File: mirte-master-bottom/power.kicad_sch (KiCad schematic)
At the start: 14 parts, among them J10 charger, J11 switch, J3 battery, K2 SANYOU_SRD_Form_A, U1 INA226, U2 TPS82130

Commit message: verder v3 pcb
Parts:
- removed K2: SANYOU_SRD_Form_A, Relay_THT:Relay_SPST_SANYOU_SRD_Series_Form_A, symbol Relay:SANYOU_SRD_Form_A
- added C10: 1000uF, Capacitor_THT:CP_Radial_D10.0mm_P3.50mm, symbol Device:C_Polarized
- added C8: 10uF, Capacitor_SMD:C_0805_2012Metric, symbol Device:C
- added C9: 100nF, Capacitor_SMD:C_0805_2012Metric, symbol Device:C
- added D2, D3: LED, LED_SMD:LED_0805_2012Metric, symbol Device:LED
- added F4: Polyfuse, Fuse:Fuse_1812_4532Metric, symbol Device:Polyfuse
- added J12: USB_A, Connector_USB:USB_A_Molex_67643_Horizontal, symbol Connector:USB_A
- added J2: Conn_02x02_Odd_Even, easyeda2:mini560, symbol Connector_Generic:Conn_02x02_Odd_Even
- added Q3: SiA449DJ, Package_TO_SOT_SMD:Vishay_PowerPAK_SC70-6L_Single, symbol Transistor_FET:SiA449DJ
- added Q5: Si2302CDS-T1-GE3, easyeda2:SOT-23_L2.9-W1.3-P1.90-LS2.4-BR, symbol easyeda:Si2302CDS-T1-GE3
- added R32, R33: 10k, Resistor_SMD:R_0805_2012Metric, symbol Device:R
- added R34: 220, Resistor_SMD:R_0805_2012Metric, symbol Device:R
- added R35: 32k, Resistor_SMD:R_0805_2012Metric, symbol Device:R
- added R4: ~700R, Resistor_SMD:R_0805_2012Metric, symbol Device:R
- added R8: ~600R, Resistor_SMD:R_0805_2012Metric, symbol Device:R
- added SW1: SW_DIP_x01, symbol Switch:SW_DIP_x01
- added U10, U11, U3, U4: 726386-2, easyeda2:CONN-TH_726386-2, symbol easyeda:726386-2
- C1, C2, C3, U2: now not fitted
- J11: value switch -> Ext 12v out; now not fitted
- R15: footprint (none) -> Resistor_SMD:R_1206_3216Metric
- R16, R17, R18: footprint (none) -> Resistor_SMD:R_0805_2012Metric; now not fitted
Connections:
- net +12V: now also J11.1 (Pin_1), C10.1, J2.2 (Pin_2), R4.1
- net +5V: now also F4.1, J2.4 (Pin_4)
- net GND: now also J11.2 (Pin_2), U1.1 (A1), U1.2 (A0), C10.2, C8.2, C9.2, D2.1 (K), D3.1 (K), J12.4 (GND), J12.5 (Shield), J2.1 (Pin_1), J2.3 (Pin_3), Q5.2 (S), R33.1, U11.1
- net VIN: now also Q3.4 (S), R32.2, SW1.1, U4.1; no longer R15.1, U1.10 (Vin+), U1.8 (Vbus)
- new net: D2.2 (A), R4.2
- new net: Q3.3 (G), Q5.3 (D), R32.1
- new net: C8.1, C9.1, F4.2, J12.1 (VBUS), R8.1
- new net: Q5.1 (G), R33.2, R34.2, R35.1
- new net: D3.2 (A), R8.2
- new net PWR_IN_SIG: R34.1, U10.1
- new net VIN_SWITCHED: Q3.1 (D), R15.1, R35.2, SW1.2, U1.10 (Vin+), U1.8 (Vbus), U3.1
- no-connect marks 0 -> 3
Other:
- note added: "PWR light"
- note added: "TODO: check pwr req"
- note added: "of de 469 miss?"
- note added: "switch"
- note removed: "TODO: switch"

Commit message: v3 mm: power upd
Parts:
- added C11: 2.2uF, Capacitor_SMD:C_0805_2012Metric, symbol Device:C
- added D4: 3v3, Diode_SMD:D_0805_2012Metric, symbol Device:D_Zener
- added Q2: Si2302CDS-T1-GE3, easyeda2:SOT-23_L2.9-W1.3-P1.90-LS2.4-BR, symbol easyeda:Si2302CDS-T1-GE3
- added U12: TPS2419D, symbol Power_Management:TPS2419D
- R35: value 32k -> 10k
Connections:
- net GND: now also D4.2 (A), U12.1 (RSET), U12.3 (GND), U12.4 (GND)
- net at Q5.1 (G), R33.2, R34.2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: now also D4.1 (K)
- new net: Q2.1 (G), U12.5 (GATE)
- new net: Q2.3 (D), U12.6 (C)
- new net: C11.1, Q2.2 (S), U12.7 (A)
- new net: C11.2, U12.8 (BYP)
- no-connect marks 3 -> 4
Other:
- note added: "10k: VIN>7v 32k if no D4"
- note added: "Idea: On power-on, no energy flowing anywhere SW1 starts the system Q3 switches the main power when Q5 is on Q5 Gate should be around 3v3 if VIN_SWITCHED is high D4 (zener diode) keeps it at max 3v3 When the microcontroller wants to turn off the power, it switches PWR_IN_SIG to low, turnin off Q5, turning off Q3 R33 is to deplete Q5 when VIN_SWITCHED is off R32 is to deplete Q3 when Q3 is off"
- note added: "N MOSFET"
- note added: "P MOSFET"

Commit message: upd main layout v3
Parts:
- removed U10, U11, U3, U4: 726386-2, easyeda2:CONN-TH_726386-2, symbol easyeda:726386-2
- added C12: 100nF, Capacitor_SMD:C_0805_2012Metric, symbol Device:C
- added J18: Conn_01x02_Pin, Connector_JST:JST_XH_B2B-XH-AM_1x02_P2.50mm_Vertical, symbol Connector:Conn_01x02_Pin
- added J19: 5V, Connector_PinHeader_2.54mm:PinHeader_1x02_P2.54mm_Vertical, symbol Connector:Conn_01x02_Pin
- added J20: 12V, Connector_PinHeader_2.54mm:PinHeader_1x02_P2.54mm_Vertical, symbol Connector:Conn_01x02_Pin
- added J21: 3V3, Connector_PinHeader_2.54mm:PinHeader_1x02_P2.54mm_Vertical, symbol Connector:Conn_01x02_Pin
- added J4: VIN, Connector_PinHeader_2.54mm:PinHeader_1x02_P2.54mm_Vertical, symbol Connector:Conn_01x02_Pin
- added J9: switch, TerminalBlock_Phoenix:TerminalBlock_Phoenix_PT-1,5-2-5.0-H_1x02_P5.00mm_Horizontal, symbol Connector:Screw_Terminal_01x02
- C11, Q2: now not fitted
- J2: value Conn_02x02_Odd_Even -> 5vConverter
- U12: footprint (none) -> Package_SO:SOIC-8_3.9x4.9mm_P1.27mm; now not fitted
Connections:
- net +12V: now also J20.1 (Pin_1)
- net +5V: now also C12.1, J19.1 (Pin_1)
- net GND: now also C12.2, J18.2 (Pin_2), J19.2 (Pin_2), J20.2 (Pin_2), J21.2 (Pin_2), J4.2 (Pin_2)
- net PWR_IN_SIG: now also J18.1 (Pin_1); no longer R34.1
- net VIN: now also J4.1 (Pin_1), J9.2 (Pin_2)
- net VIN_SWITCHED: now also J9.1 (Pin_1)
- new net +3V3: J21.1 (Pin_1)
- new net RELAY_PWR: R34.1

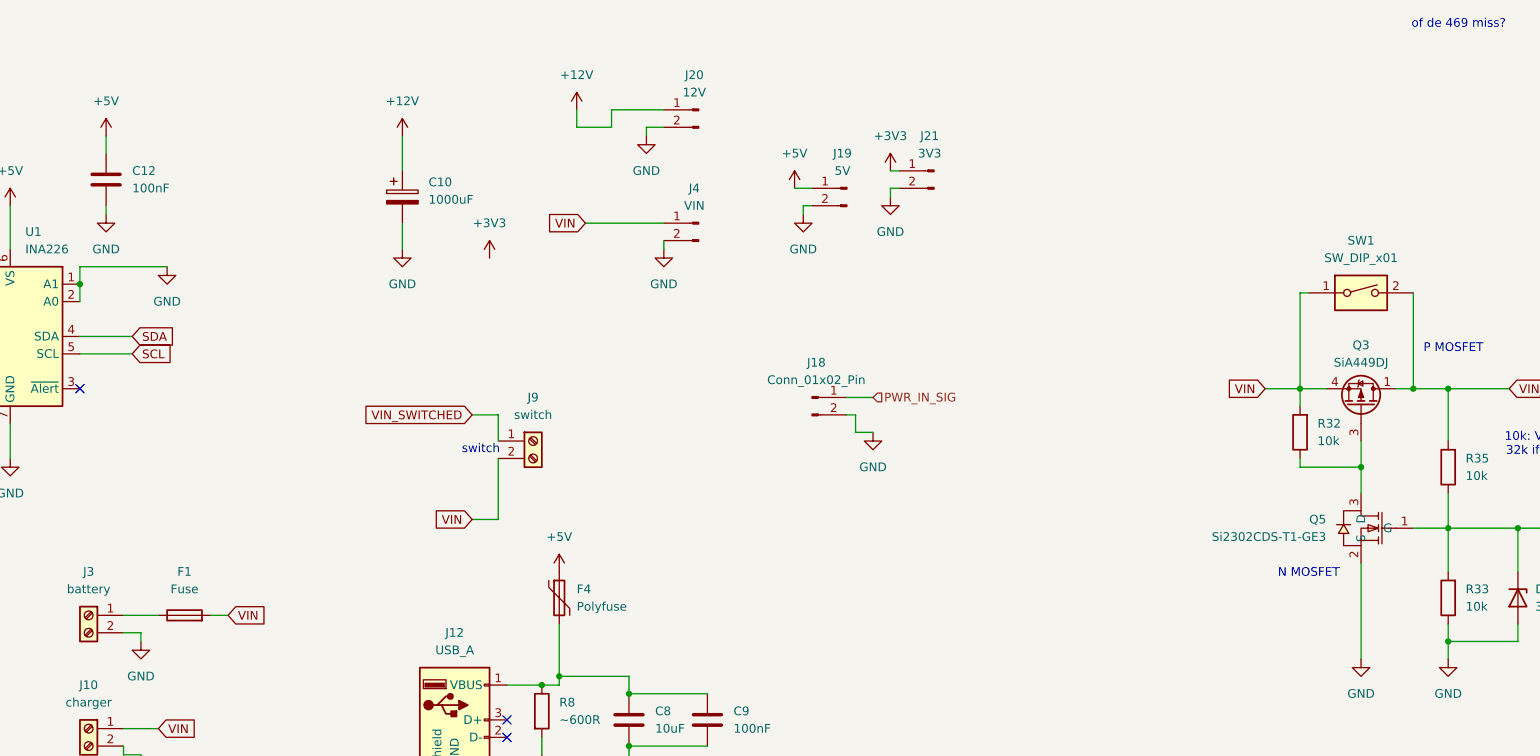
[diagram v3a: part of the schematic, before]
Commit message: ordered pcb main v3
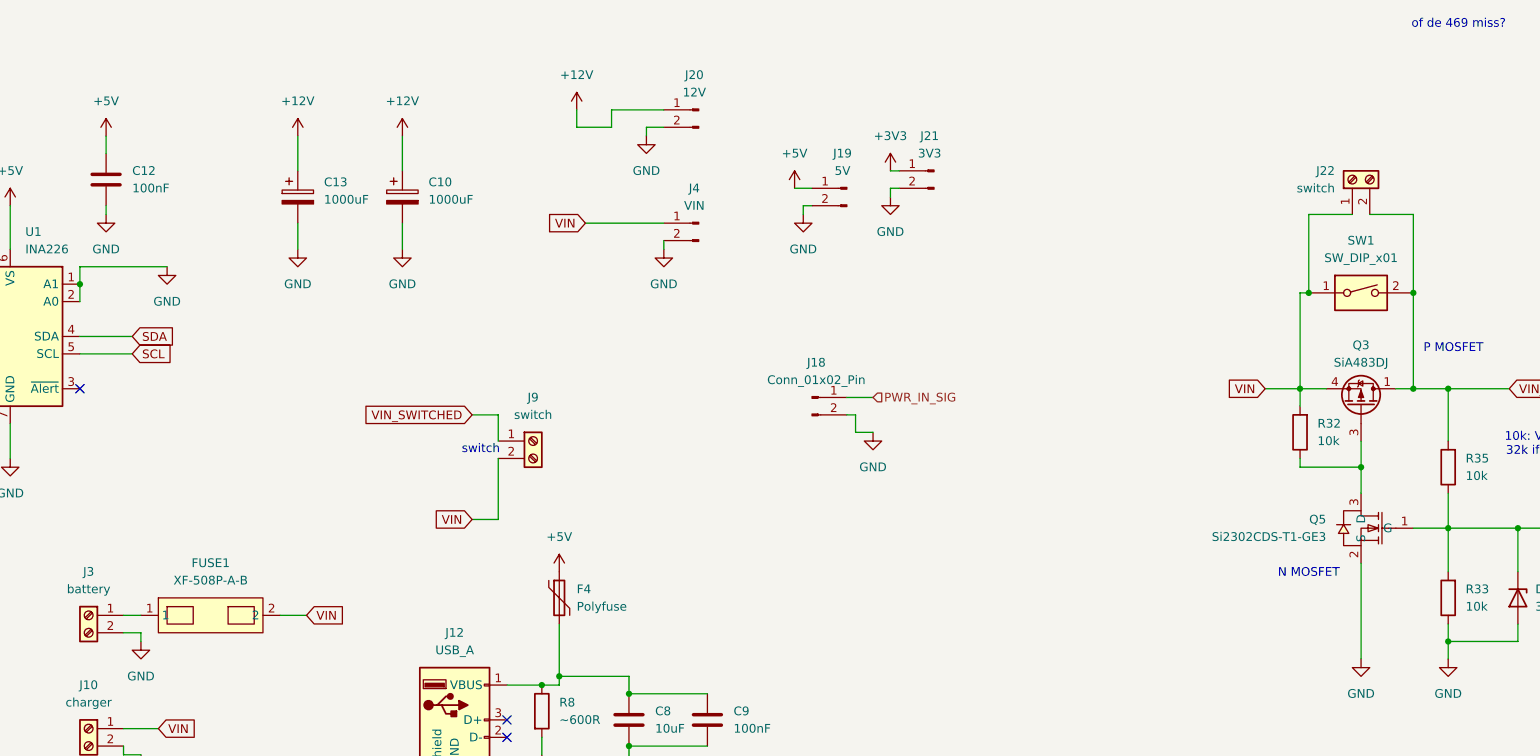
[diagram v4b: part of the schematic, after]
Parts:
- removed F1: Fuse, Fuse:Fuseholder_Blade_ATO_Littelfuse_Pudenz_2_Pin, symbol Device:Fuse
- added C13: 1000uF, Capacitor_THT:CP_Radial_D10.0mm_P3.50mm, symbol Device:C_Polarized
- added FUSE1: XF-508P-A-B, easyeda2:FUSE-TH_XF-508P-A-B, symbol easyeda:XF-508P-A-B
- added J22: switch, TerminalBlock_Phoenix:TerminalBlock_Phoenix_PT-1,5-2-5.0-H_1x02_P5.00mm_Horizontal, symbol Connector:Screw_Terminal_01x02
- Q3: value SiA449DJ -> SiA483DJ
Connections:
- net +12V: now also C13.1
- net GND: now also C13.2
- net VIN: now also FUSE1.2, J22.1 (Pin_1)
- net VIN_SWITCHED: now also J22.2 (Pin_2)
- net at J3.1 (Pin_1): now also FUSE1.1

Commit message: Upd power and hbridge, rm polyfuse
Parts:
- removed D4: 3v3, Diode_SMD:D_0805_2012Metric, symbol Device:D_Zener
- removed F4: Polyfuse, Fuse:Fuse_1812_4532Metric, symbol Device:Polyfuse
- removed Q5: Si2302CDS-T1-GE3, easyeda2:SOT-23_L2.9-W1.3-P1.90-LS2.4-BR, symbol easyeda:Si2302CDS-T1-GE3
- removed R34: 220, Resistor_SMD:R_0805_2012Metric, symbol Device:R
- added D4, D9: DSK310, easyeda:SOD-123FL_L2.8-W1.9-LS3.7-RD, symbol easyeda:DSK310_C28646289
- added R19: 12k?, Resistor_SMD:R_0805_2012Metric, symbol Device:R
- added R20, R21: 390, Resistor_SMD:R_0805_2012Metric, symbol Device:R
- added R22: fix_dnp, Resistor_SMD:R_0805_2012Metric, symbol Device:R
- added U5: TL431BIDBZR, easyeda:SOT-23-3_L2.9-W1.3-P1.90-LS2.4-BR, symbol easyeda:TL431BIDBZR
- FUSE1: footprint easyeda2:FUSE-TH_XF-508P-A-B -> easyeda:FUSE-TH_XF-508P-A-B
- J2: footprint easyeda2:mini560 -> easyeda:mini560
- R32: value 10k -> 12k
- R33: value 10k -> 3k9
- R35: value 10k -> 390
- R4: value ~700R -> 1k2
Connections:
- net +12V: now also U1.8 (Vbus)
- net +5V: now also C8.1, C9.1, J12.1 (VBUS), R8.1
- net GND: now also U5.3 (ANODE)
- net RELAY_PWR: now also D9.1
- net VIN_SWITCHED: now also R19.2, R22.2; no longer R35.2, U1.8 (Vbus)
- net at Q3.3 (G), R32.1: now also R20.2
- net at R33.2: now also R21.1, U5.2 (REF); no longer R35.1
- new net: D9.2, R21.2, R35.1
- new net: D4.2, R19.1, R22.1, R35.2
- new net: D4.1, R20.1, U5.1 (CATHODE)
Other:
- note added: "TODO: dit opnieuw routen, schema al beter nav layout example"
- note added: "turn on 0.7-3.3V@2V-5V turn off 0.6-2V@2V-5V off-trigger @ V-in = 9V 9V/1.5V = 1:4"
- moved on the sheet: R33, R35

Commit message: Cleanups and checks mm bottom v3
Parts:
- R15: footprint Resistor_SMD:R_1206_3216Metric -> Resistor_SMD:R_0805_2012Metric
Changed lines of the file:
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@@
 	)
 	(symbol
-		(lib_name "GND_1")
 		(lib_id "power:GND")
 		(at 101.6 87.63 0)
@@
 	)
 	(symbol
-		(lib_name "GND_1")
 		(lib_id "power:GND")
 		(at 120.65 125.73 0)
@@
 	)
 	(symbol
-		(lib_name "GND_1")
 		(lib_id "power:GND")
 		(at 156.21 113.03 0)
@@
 	)
 	(symbol
-		(lib_name "GND_1")
 		(lib_id "power:GND")
 		(at 156.21 129.54 0)
@@
 	)
 	(symbol
-		(lib_name "GND_1")
 		(lib_id "power:GND")
 		(at 137.16 86.36 0)
@@
 	)
 	(symbol
-		(lib_name "GND_1")
 		(lib_id "power:GND")
 		(at 151.13 50.8 0)
@@
 	)
 	(symbol
-		(lib_name "GND_1")
 		(lib_id "power:GND")
 		(at 160.02 58.42 0)
@@
 	)
 	(symbol
-		(lib_name "+5V_1")
 		(lib_id "power:+5V")
 		(at 251.46 46.99 0)
@@
 	)
 	(symbol
-		(lib_name "GND_1")
 		(lib_id "power:GND")
 		(at 152.4 160.02 0)
@@
 	)
 	(symbol
-		(lib_name "+5V_1")
 		(lib_id "power:+5V")
 		(at 151.13 39.37 0)
@@
 	)
 	(symbol
-		(lib_name "+5V_1")
 		(lib_id "power:+5V")
 		(at 50.8 107.95 0)
@@
 	)
 	(symbol
-		(lib_name "GND_1")
 		(lib_id "power:GND")
 		(at 71.12 138.43 0)
@@
 	)
 	(symbol
-		(lib_name "GND_1")
 		(lib_id "power:GND")
 		(at 107.95 135.89 0)
@@
 	)
 	(symbol
-		(lib_name "+5V_1")
 		(lib_id "power:+5V")
 		(at 104.14 111.76 0)
@@
 			)
 		)
-		(property "Footprint" "Resistor_SMD:R_1206_3216Metric"
+		(property "Footprint" "Resistor_SMD:R_0805_2012Metric"
 			(at 111.252 72.39 90)
 			(effects
@@
 	)
 	(symbol
-		(lib_name "GND_1")
 		(lib_id "power:GND")
 		(at 91.44 133.35 0)
@@
 			)
 		)
-		(property "Description" ""
+		(property "Description" "Power symbol creates a global label with name \"GND\" , ground"
 			(at 214.63 140.97 0)
 			(effects
@@
 	)
 	(symbol
-		(lib_name "+5V_1")
 		(lib_id "power:+5V")
 		(at 137.16 49.53 0)
@@
 			)
 		)
-		(property "Description" ""
+		(property "Description" "Power symbol creates a global label with name \"GND\" , ground"
 			(at 49.53 67.31 0)
 			(effects

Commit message: add pwr sens sys, upd kicad9
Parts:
- removed J9: switch, TerminalBlock_Phoenix:TerminalBlock_Phoenix_PT-1,5-2-5.0-H_1x02_P5.00mm_Horizontal, symbol Connector:Screw_Terminal_01x02
- added D11: SB2080L_C41424807, easyeda:TO-277B-3_L5.4-W4.1-P1.85-LS6.5-TR, symbol easyeda:SB2080L_C41424807
- added D12: BAT54SLT1G, easyeda:SOT-23_L2.9-W1.3-P1.90-LS2.4-BR, symbol easyeda:BAT54SLT1G
- added R52: 1k2, Resistor_SMD:R_0805_2012Metric, symbol Device:R
- added R53: 3k, Resistor_SMD:R_0805_2012Metric, symbol Device:R
- added R54: 390, Resistor_SMD:R_0805_2012Metric, symbol Device:R
- J18: now not fitted; now left out of the parts list
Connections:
- net +3V3: now also D12.2 (C)
- net GND: now also D12.1 (A), R52.2; no longer J18.2 (Pin_2)
- net PWR_IN_SIG: now also R54.1; no longer J18.1 (Pin_1)
- net VIN_SWITCHED: now also D11.2; no longer J22.2 (Pin_2)
- new net: D12.3 (A/C), R52.1, R53.1, R54.2
- new net pwr_sense_12: D11.1, D11.3, J22.2 (Pin_2), R53.2

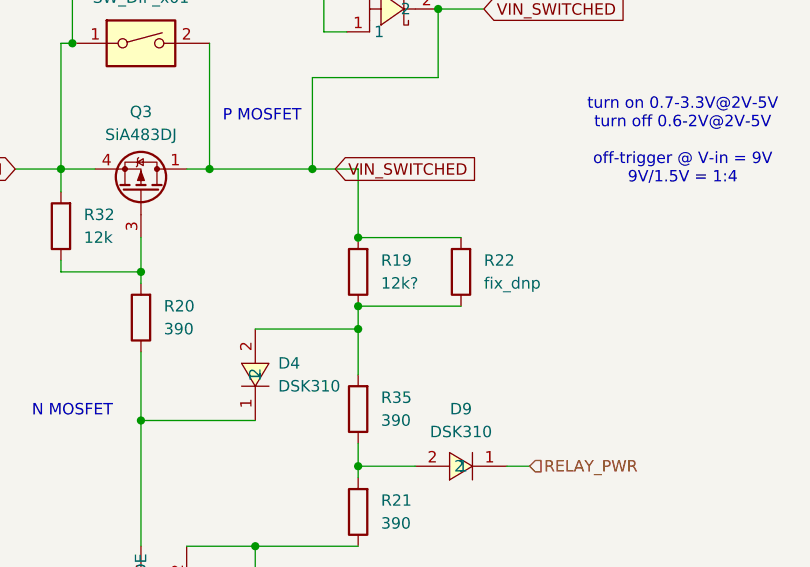
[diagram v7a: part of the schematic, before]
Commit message: Change switch resistor to 10k for later turn off + add sim
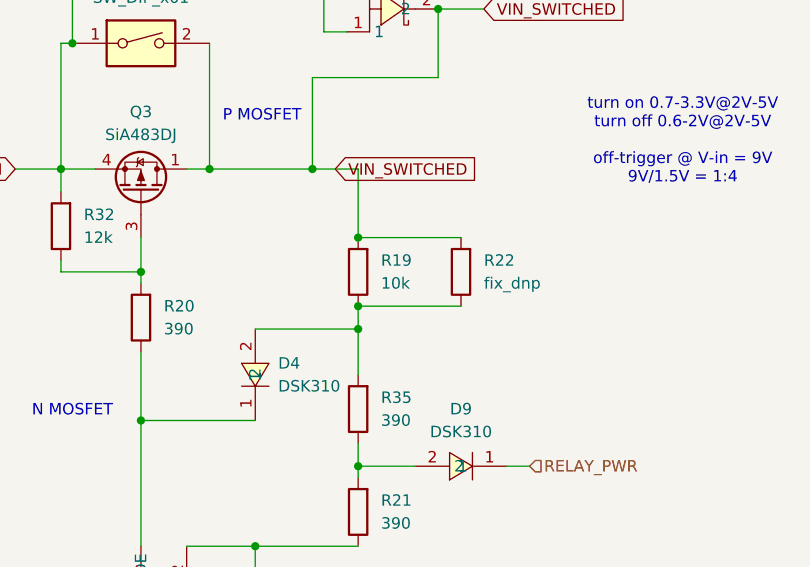
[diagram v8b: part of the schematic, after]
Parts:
- R19: value 12k? -> 10k
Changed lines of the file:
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@@
 			)
 		)
-		(property "Value" "12k?"
+		(property "Value" "10k"
 			(at 360.68 88.8999 0)
 			(effects
